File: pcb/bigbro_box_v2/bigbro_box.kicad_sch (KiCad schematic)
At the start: 41 parts, among them J1 CT_AMP, J2 Display, J3 Mains, J4 UART flashing, J5 Conn_01x02, J6 Relay, K1 G5LE-1, Q1 ADC114YUQ, Q2 BSS138, Q3 MMBT3906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

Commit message: Remove unneeded pulldown.
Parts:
- removed R6: 10k, Resistor_SMD:R_0603_1608Metric_Pad0.98x0.95mm_HandSolder, symbol Device:R_Small
- D1: value D_Small -> 1N4148
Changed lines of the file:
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@@
   (junction (at 176.53 32.766) (diameter 1.016) (color 0 0 0 0)
-  )
-  (junction (at 36.83 134.62) (diameter 0) (color 0 0 0 0)
-  )
-  (junction (at 38.1 127) (diameter 0) (color 0 0 0 0)
   )
   (junction (at 176.53 23.114) (diameter 1.016) (color 0 0 0 0)
@@
     (stroke (width 0) (type default))
   )
-  (wire (pts (xy 35.56 134.62) (xy 35.56 133.35))
-    (stroke (width 0) (type default))
-  )
-  (wire (pts (xy 36.83 134.62) (xy 35.56 134.62))
-    (stroke (width 0) (type default))
-  )
-  (wire (pts (xy 38.1 133.35) (xy 38.1 134.62))
-    (stroke (width 0) (type default))
-  )
-  (wire (pts (xy 38.1 134.62) (xy 36.83 134.62))
+  (wire (pts (xy 35.56 133.35) (xy 35.56 135.89))
     (stroke (width 0) (type default))
   )
@@
     (stroke (width 0) (type default))
   )
-  (wire (pts (xy 29.21 127) (xy 38.1 127))
-    (stroke (width 0) (type default))
-  )
-  (wire (pts (xy 38.1 127) (xy 48.26 127))
+  (wire (pts (xy 29.21 127) (xy 48.26 127))
     (stroke (width 0) (type default))
   )
@@
     (stroke (width 0) (type default))
   )
-  (wire (pts (xy 38.1 127) (xy 38.1 128.27))
-    (stroke (width 0) (type default))
-  )
   (wire (pts (xy 22.86 92.71) (xy 24.13 92.71))
     (stroke (width 0) (type default))
@@
   )
   (wire (pts (xy 351.79 91.44) (xy 351.79 96.52))
-    (stroke (width 0) (type default))
-  )
-  (wire (pts (xy 36.83 134.62) (xy 36.83 135.89))
     (stroke (width 0) (type default))
   )
@@
     )
   )
-  (symbol (lib_id "Device:R_Small") (at 38.1 130.81 0) (unit 1)
-    (in_bom yes) (on_board yes) (dnp no)
-    (property "Reference" "R6" (at 39.37 129.5399 0)
-      (effects (font (size 1.27 1.27)) (justify left))
-    )
-    (property "Value" "10k" (at 39.37 132.0799 0)
-      (effects (font (size 1.27 1.27)) (justify left))
-    )
-    (property "Footprint" "Resistor_SMD:R_0603_1608Metric_Pad0.98x0.95mm_HandSolder" (at 38.1 130.81 0)
-      (effects (font (size 1.27 1.27)) hide)
-    )
-    (property "Datasheet" "~" (at 38.1 130.81 0)
-      (effects (font (size 1.27 1.27)) hide)
-    )
-    (pin "1")
-    (pin "2")
-    (instances
-      (project "bigbro_box"
-        (path "/212a0d71-cc7b-49f8-b4ca-a935e5355dca"
-          (reference "R6") (unit 1)
-        )
-      )
-    )
-  )
   (symbol (lib_id "Device:R_Small") (at 165.1 85.09 0) (mirror y) (unit 1)
     (in_bom yes) (on_board yes) (dnp no)
@@
       (effects (font (size 1.27 1.27)))
     )
-    (property "Value" "D_Small" (at 331.47 83.82 0)
+    (property "Value" "1N4148" (at 331.47 83.82 0)
       (effects (font (size 1.27 1.27)))
     )
@@
     )
   )
-  (symbol (lib_id "power:GND") (at 36.83 135.89 0) (unit 1)
-    (in_bom yes) (on_board yes) (dnp no)
-    (property "Reference" "#PWR0103" (at 36.83 142.24 0)
-      (effects (font (size 1.27 1.27)) hide)
-    )
-    (property "Value" "GND" (at 36.83 140.97 0)
-      (effects (font (size 1.27 1.27)))
-    )
-    (property "Footprint" "" (at 36.83 135.89 0)
-      (effects (font (size 1.27 1.27)) hide)
-    )
-    (property "Datasheet" "" (at 36.83 135.89 0)
-      (effects (font (size 1.27 1.27)) hide)
-    )
+  (symbol (lib_id "power:GND") (at 35.56 135.89 0) (unit 1)
+    (in_bom yes) (on_board yes) (dnp no)
+    (property "Reference" "#PWR0103" (at 35.56 142.24 0)
+      (effects (font (size 1.27 1.27)) hide)
+    )
+    (property "Value" "GND" (at 35.56 140.97 0)
+      (effects (font (size 1.27 1.27)))
+    )
+    (property "Footprint" "" (at 35.56 135.89 0)
+      (effects (font (size 1.27 1.27)) hide)
+    )
+    (property "Datasheet" "" (at 35.56 135.89 0)
+      (effects (font (size 1.27 1.27)) hide)
+    )

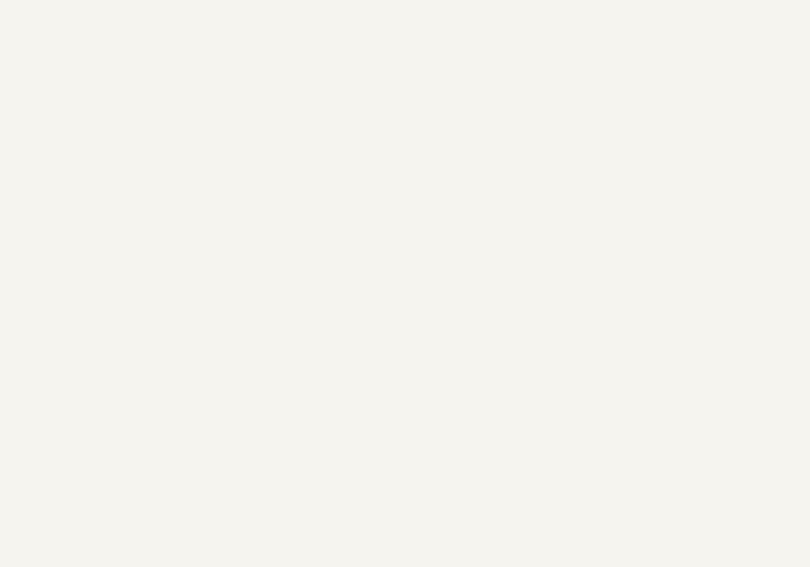
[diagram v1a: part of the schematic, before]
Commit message: Add local libs/footprints. Add GND testpoint.
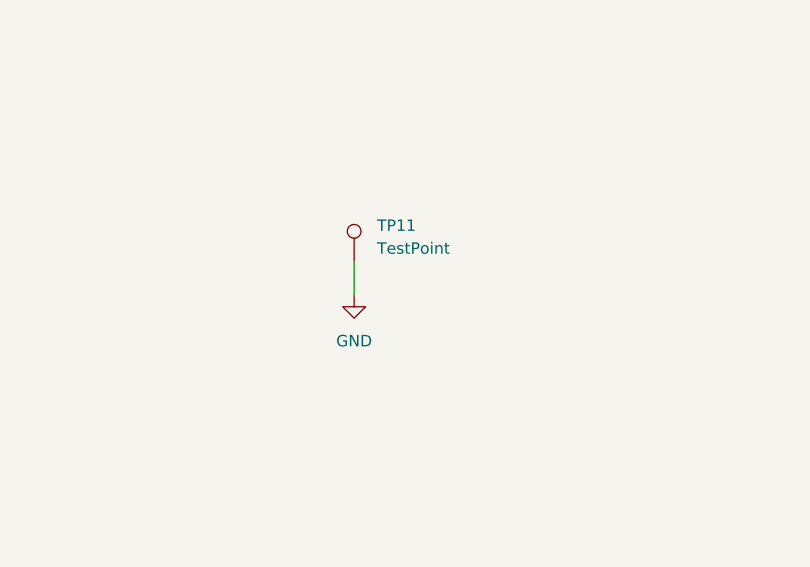
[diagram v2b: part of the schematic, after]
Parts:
- added TP11: TestPoint, symbol Connector:TestPoint
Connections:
- net GND: now also TP11.1
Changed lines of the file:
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@@
     (stroke (width 0) (type solid))
+  )
+  (wire (pts (xy 242.57 88.9) (xy 242.57 92.71))
+    (stroke (width 0) (type default))
   )
   (wire (pts (xy 88.9 62.23) (xy 91.44 62.23))
@@
     )
   )
+  (symbol (lib_id "Connector:TestPoint") (at 242.57 88.9 0) (unit 1)
+    (in_bom yes) (on_board yes) (dnp no) (fields_autoplaced)
+    (property "Reference" "TP11" (at 245.11 84.963 0)
+      (effects (font (size 1.27 1.27)) (justify left))
+    )
+    (property "Value" "TestPoint" (at 245.11 87.503 0)
+      (effects (font (size 1.27 1.27)) (justify left))
+    )
+    (property "Footprint" "" (at 247.65 88.9 0)
+      (effects (font (size 1.27 1.27)) hide)
+    )
+    (property "Datasheet" "~" (at 247.65 88.9 0)
+      (effects (font (size 1.27 1.27)) hide)
+    )
+    (pin "1")
+    (instances
+      (project "bigbro_box"
+        (path "/212a0d71-cc7b-49f8-b4ca-a935e5355dca"
+          (reference "TP11") (unit 1)
+        )
+      )
+    )
+  )
   (symbol (lib_id "Device:R_Small") (at 35.56 130.81 0) (unit 1)
     (in_bom yes) (on_board yes) (dnp no)
@@
         )
       )
+    )
+  )
+  (symbol (lib_name "GND_1") (lib_id "power:GND") (at 242.57 92.71 0) (unit 1)
+    (in_bom yes) (on_board yes) (dnp no) (fields_autoplaced)
+    (property "Reference" "#PWR08" (at 242.57 99.06 0)
+      (effects (font (size 1.27 1.27)) hide)
+    )
+    (property "Value" "GND" (at 242.57 97.79 0)
+      (effects (font (size 1.27 1.27)))
+    )
+    (property "Footprint" "" (at 242.57 92.71 0)
+      (effects (font (size 1.27 1.27)) hide)
+    )
+    (property "Datasheet" "" (at 242.57 92.71 0)
+      (effects (font (size 1.27 1.27)) hide)
+    )
+    (pin "1")
+    (instances
+      (project "bigbro_box"
+        (path "/212a0d71-cc7b-49f8-b4ca-a935e5355dca"
+          (reference "#PWR08") (unit 1)
+        )
+      )

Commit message: Change to RDM6300, etc.
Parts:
- removed unit 2 of Q1
- removed U5: RF125-PS, mylib:rf125ps, symbol rf125ps:RF125-PS
- removed U6: 74LVC1T45, Package_TO_SOT_SMD:SOT-23-6, symbol 74lvc:74LVC1T45
- added D2, D3: LED, LED_SMD:LED_0603_1608Metric, symbol Device:LED
- added Q2: MMBT3904, Package_TO_SOT_SMD:SOT-23, symbol Transistor_BJT:MMBT3904
- added R6: 1K, Resistor_SMD:R_0603_1608Metric, symbol Device:R
- added R9: 330, Resistor_SMD:R_0603_1608Metric, symbol Device:R
- added unit 4 of U4
- added unit 3 of U4
- added U5: RDM6300, modules:RDM6300_B38.5x18.2mm, symbol gtrzps:RDM6300
- Q1: value ADC114YUQ -> MMBT3904; footprint Package_TO_SOT_SMD:SOT-363_SC-70-6 -> Package_TO_SOT_SMD:SOT-23; symbol Transistor_BJT:MUN5211DW1 -> Transistor_BJT:MMBT3904
- TP11: footprint (none) -> TestPoint:TestPoint_Keystone_5000-5004_Miniature
- renumbered Q2 to Q3, Q3 to Q4
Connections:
- net +3V3: now also U4.12, U4.13
- net +5V: now also D2.2 (A), U5.10 (5V), U5.4 (5V)
- net ESP_RFID_TX: now also U5.6 (TX)
- net GND: now also D3.1 (K), U4.8, U4.9, U5.3 (GND), U5.9 (GND)
- net NC: now also J6.1 (Pin_1); no longer J6.3 (Pin_3)
- net NO: now also J6.3 (Pin_3); no longer J6.1 (Pin_1)
- net card_switch: now also R9.1
- net ~{DTR}: now also Q1.2 (E), Q2.1 (B); no longer Q1.4 (E1)
- net ~{RESET}: now also Q2.3 (C)
- net ~{RTS}: now also Q1.1 (B), Q2.2 (E); no longer Q1.5 (B1)
- net at D1.2 (A), K1.2, Q3.2 (D): now also R6.2
- net at J5.2 (Pin_2): now also U5.2 (ANT2)
- net at J5.1 (Pin_1): now also U5.1 (ANT1)
- net L_in: no longer names the net of J3.1 (Pin_1)
- net L_in: now also PS1.2 (AC/N); no longer F1.1
- net N_in: no longer names the net of J3.2 (Pin_2)
- net N_in: now also F1.1; no longer PS1.2 (AC/N)
- new net: D3.2 (A), R9.2
- new net: D2.1 (K), R6.1
- no-connect marks 8 -> 13
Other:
- moved on the sheet: C3, J3, J5, TP11
